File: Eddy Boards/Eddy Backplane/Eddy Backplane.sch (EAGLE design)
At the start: 89 parts, among them J1 USB_MINI-B_SMT, P1 39-30-02_S, P2 RB1-125BAG1A, P3 39-30-04_S, Q1 310mA/60V/1.6Ω, Q2 310mA/60V/1.6Ω, Q3 310mA/60V/1.6Ω, Q4 310mA/60V/1.6Ω, Q5 310mA/60V/1.6Ω, Q6 310mA/60V/1.6Ω, Q7 310mA/60V/1.6Ω, Q8 310mA/60V/1.6Ω, U1 W5500, U2 STM32F405RGT6, Y2 12MHz, Y3 32.768kHz

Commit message: Eddy backplane *mostly* complete. Just some minor things
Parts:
- removed 16MHZ, 32.768KHZ: (no value), SparkFun-Clocks:CRYSTALPTH-HC49US
- removed C10, C11, C12, C9: (no value), rcl:C-EUC0603
- removed C3, C8: 2.2 uF, rcl:C-EUC0603
- removed U$4: STM32F405RGT6, SparkFun-IC-Microcontroller:STM32F405RG
- added C25, C26, C27: (no value), rcl:C-EUC0603
- added R2, R3, R5, R6: (no value), rcl:R-US_R0603
- C7: value 0.1 uF -> (none)
- renumbered R24 to R1
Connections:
- removed net +3V3: C23.1, C24.1, R27.2, SWDIO/SWDCLK/RESET.1, SWDIO/SWDCLK/RESET.2, U1.AVDD, U1.VDD, U2.VDD, U2.VDDA
- removed net N$1: C3.1, U$4.VCAP1
- removed net N$2: C8.1, U$4.VCAP2
- removed net N$3: 32.768KHZ.1, C11.1, U$4.PC14
- removed net N$5: 16MHZ.1, C9.1, U$4.PH0
- removed net N$6: 32.768KHZ.2, C12.1, U$4.PC15
- removed net N$7: 16MHZ.2, C10.1, U$4.PH1
- new net N$22: C25.2, R5.2, R6.2
- new net N$23: P2.TD+, R3.2, U1.TXP
- new net N$24: P2.TD-, R2.2, U1.TXN
- new net N$25: C26.2, P2.RD+
- new net N$26: C26.1, R5.1, U1.RXP
- new net N$27: C27.2, R6.1, U1.RXN
- new net N$28: C27.1, P2.RD-
- net 3.3V: now also C23.1, C24.1, P2.CT, R1.2, R2.1, R23.2, R27.2, R3.1, SWDIO/SWDCLK/RESET.1, SWDIO/SWDCLK/RESET.2, U1.AVDD, U1.VDD, U2.VDD, U2.VDDA; no longer U$4.VDD1, U$4.VDD2, U$4.VDD3, U$4.VDD4, U$4.VDDA
- net GND: now also C25.1; no longer C10.2, C11.2, C12.2, C3.2, C8.2, C9.2, P2.L2, P2.L4, U$4.VSS1, U$4.VSS2, U$4.VSSA
- net KILL_SWITCH: now also SWITCH_CONNECTOR-4.P; no longer SWITCH_CONNECTOR-2.P
- net N$11: now also P2.L4; no longer R1.2
- net N$12: now also P2.L2; no longer R23.2
- net SWITCH_2: now also SWITCH_CONNECTOR-2.P; no longer SWITCH_CONNECTOR-4.P
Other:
- note added: "only five 3.3v pins on STM32, one cap deleted"
- note removed: "Ask Gus about this connection scheme for clarification"
- moved on the sheet: R23

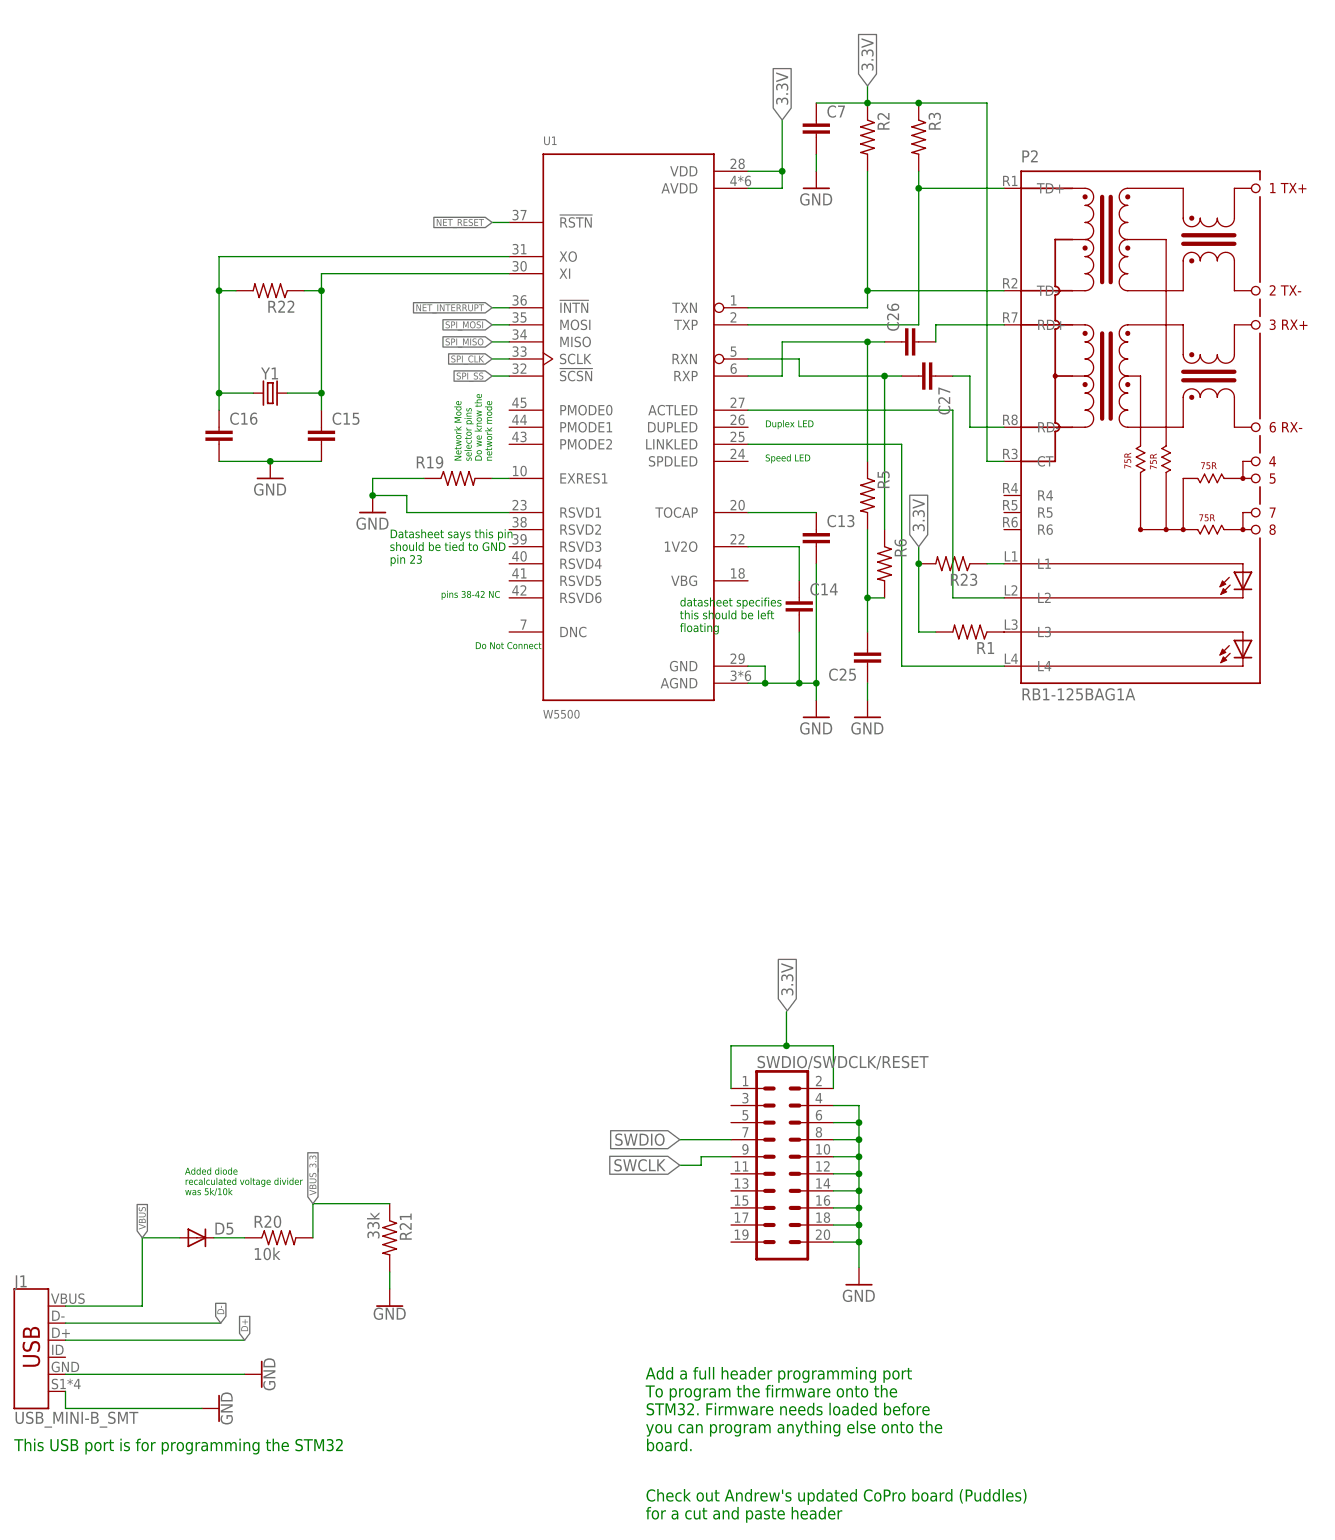
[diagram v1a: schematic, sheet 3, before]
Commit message: Eddy Backplane Ready for board review round 1
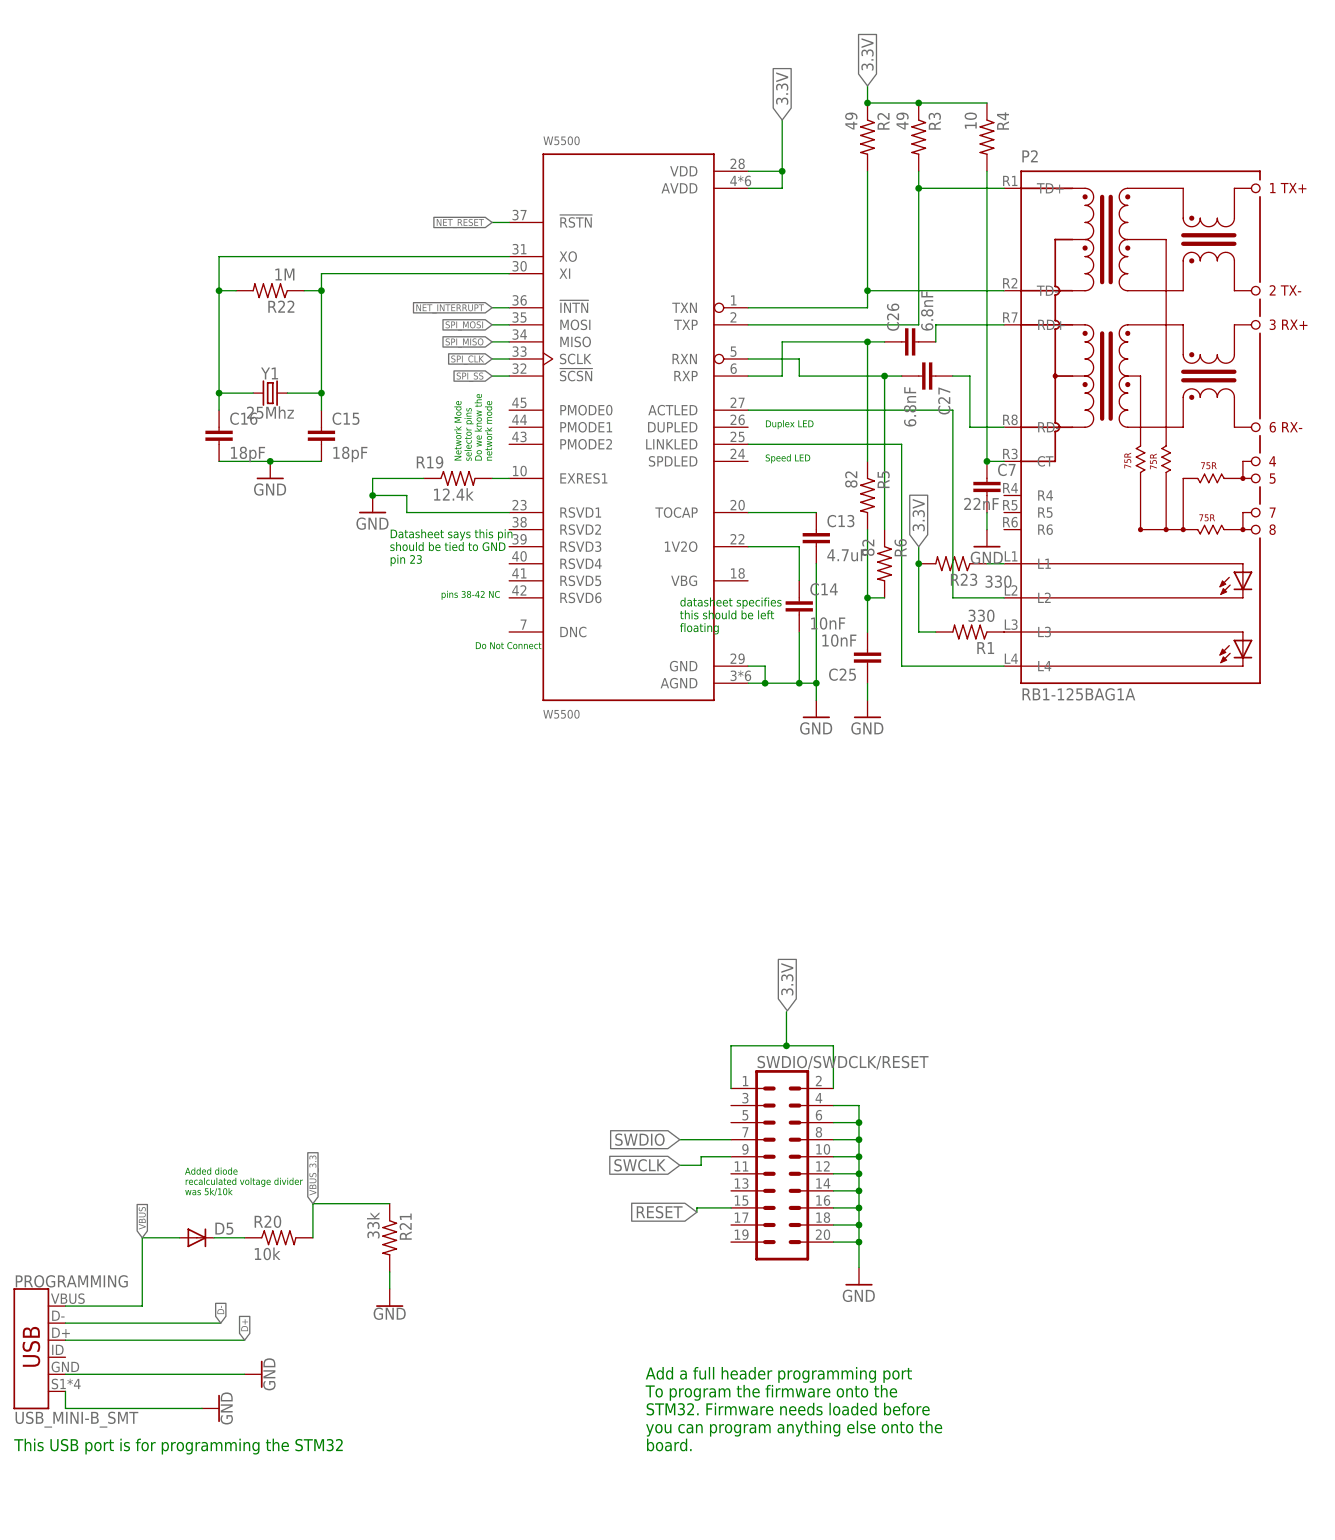
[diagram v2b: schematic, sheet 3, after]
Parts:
- added R4: 10, rcl:R-US_R0603
- C13: value (none) -> 4.7uF
- C14, C25: value (none) -> 10nF
- C15, C16: value (none) -> 18pF
- C26, C27: value (none) -> 6.8nF
- C7: value (none) -> 22nF
- R1, R23: value (none) -> 330
- R19: value (none) -> 12.4k
- R2, R3: value (none) -> 49
- R22: value (none) -> 1M
- R5, R6: value (none) -> 82
- Y1: value (none) -> 25Mhz
- renumbered J1 to PROGRAMMING, P1 to 5V_CONNECTOR, P3 to 3.3V_ROBO_I2C, S1 to RESET, U1 to W5500, U2 to STM32
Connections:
- removed net N$34: C23.2, C24.2, R27.1, RESET.2, STM32.NRST
- new net N$1: C7.1, P2.CT, R4.2
- new net RESET: C23.2, C24.2, R27.1, RESET.2, STM32.NRST, SWDIO/SWDCLK/RESET.15
- net 3.3V: now also R4.1; no longer C7.1, P2.CT
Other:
- note removed: "Check out Andrew's updated CoPro board (Puddles) for a cut and paste header"
- moved on the sheet: C7
